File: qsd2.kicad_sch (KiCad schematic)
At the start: 72 parts, among them J1 5-1814832-1, J2 5-1814832-1, J3 Conn_02x08_Odd_Even, J4 SJ-3524-SMT, J5 B4B-XH-A_LF__SN_, U1 SN74LVC1G14DBV, U10 GALI-39, U11 SN74LVC1G14DBV, U12 LM4040DBZ-2.5, U13 LM4040DBZ-2.5, U2 SN74LVC1G14DBV, U3 SN74CBT3253, U4 SN74AC74PW, U5 AD8226ARZ-R7, U6 AD8226ARZ-R7, U9 UA78M05IDCYR

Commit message: V1.2 to fab.
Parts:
- removed R16: DNP, Resistor_SMD:R_1206_3216Metric, symbol Device:R_Small_US
- removed R19: 4.7k, Resistor_SMD:R_1206_3216Metric, symbol Device:R_Small_US
- removed U12, U13: LM4040DBZ-2.5, Package_TO_SOT_SMD:SOT-23, symbol Reference_Voltage:LM4040DBZ-2.5
- added C26: 1uF, Capacitor_SMD:C_1206_3216Metric, symbol Device:C_Small
- added U7: AP7343, Package_TO_SOT_SMD:SOT-23-5, symbol AP7343-25W5-7:AP7343
- R18: value 4.7k -> 2.2k
- R23, R24: value 2.61k -> 10k
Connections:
- net REF_Q is gone; now on net REF_V: C27.1, U6.6 (REF)
- net 5V_FILT: now also C23.1, U7.1 (VIN), U7.3 (EN); no longer R18.2
- net GND: now also R18.2, C26.2, U7.2 (GND)
- net at C20.2, R14.2: now also J4.2; no longer J4.3
- net at C21.2, R13.1: now also J4.3; no longer J4.2
- net REF_I renamed REF_V
- net REF_V: now also C26.1, U7.5 (VOUT); no longer C23.1
- no-connect marks 5 -> 6
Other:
- note removed: "Option for using a single reference source"
- moved on the sheet: C23, R18

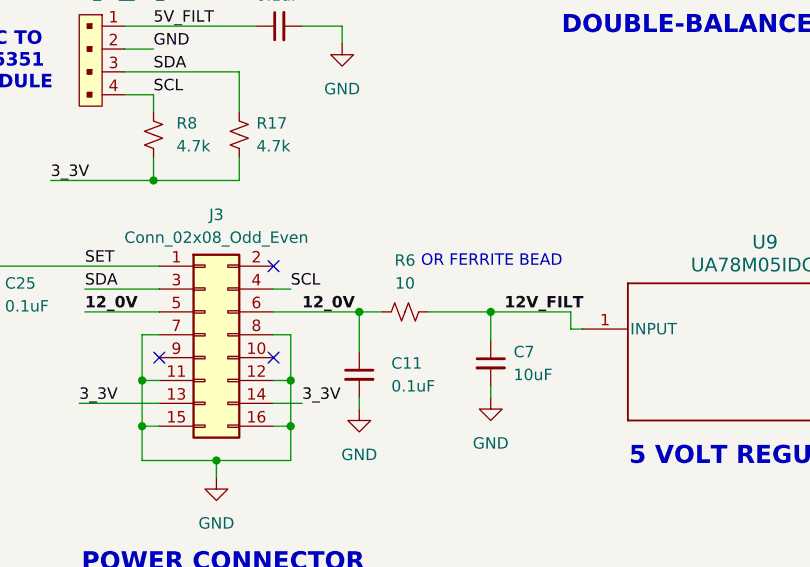
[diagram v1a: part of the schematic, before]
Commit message: Changed 10 ohm resistor to 20.  Fixed missing component value.
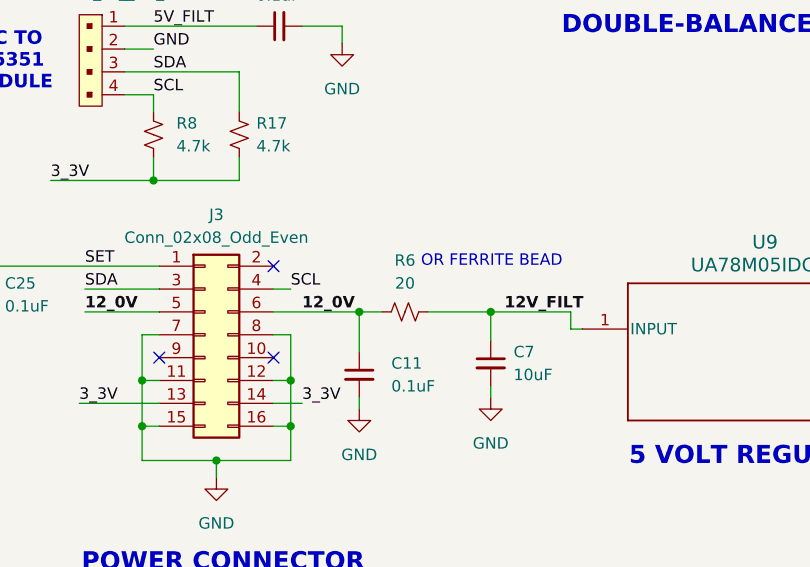
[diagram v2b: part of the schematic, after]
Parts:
- R6: value 10 -> 20
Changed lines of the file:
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@@
 	(title_block
 		(title "QSD2EZ with Divide-by-Two Quadrature Double-Balanced")
-		(date "2026-07-02")
+		(date "2026-07-21")
 		(rev "1.2")
 	)
@@
 			)
 		)
-		(property "Value" "10"
+		(property "Value" "20"
 			(at 67.945 163.83 90)
 			(show_name no)

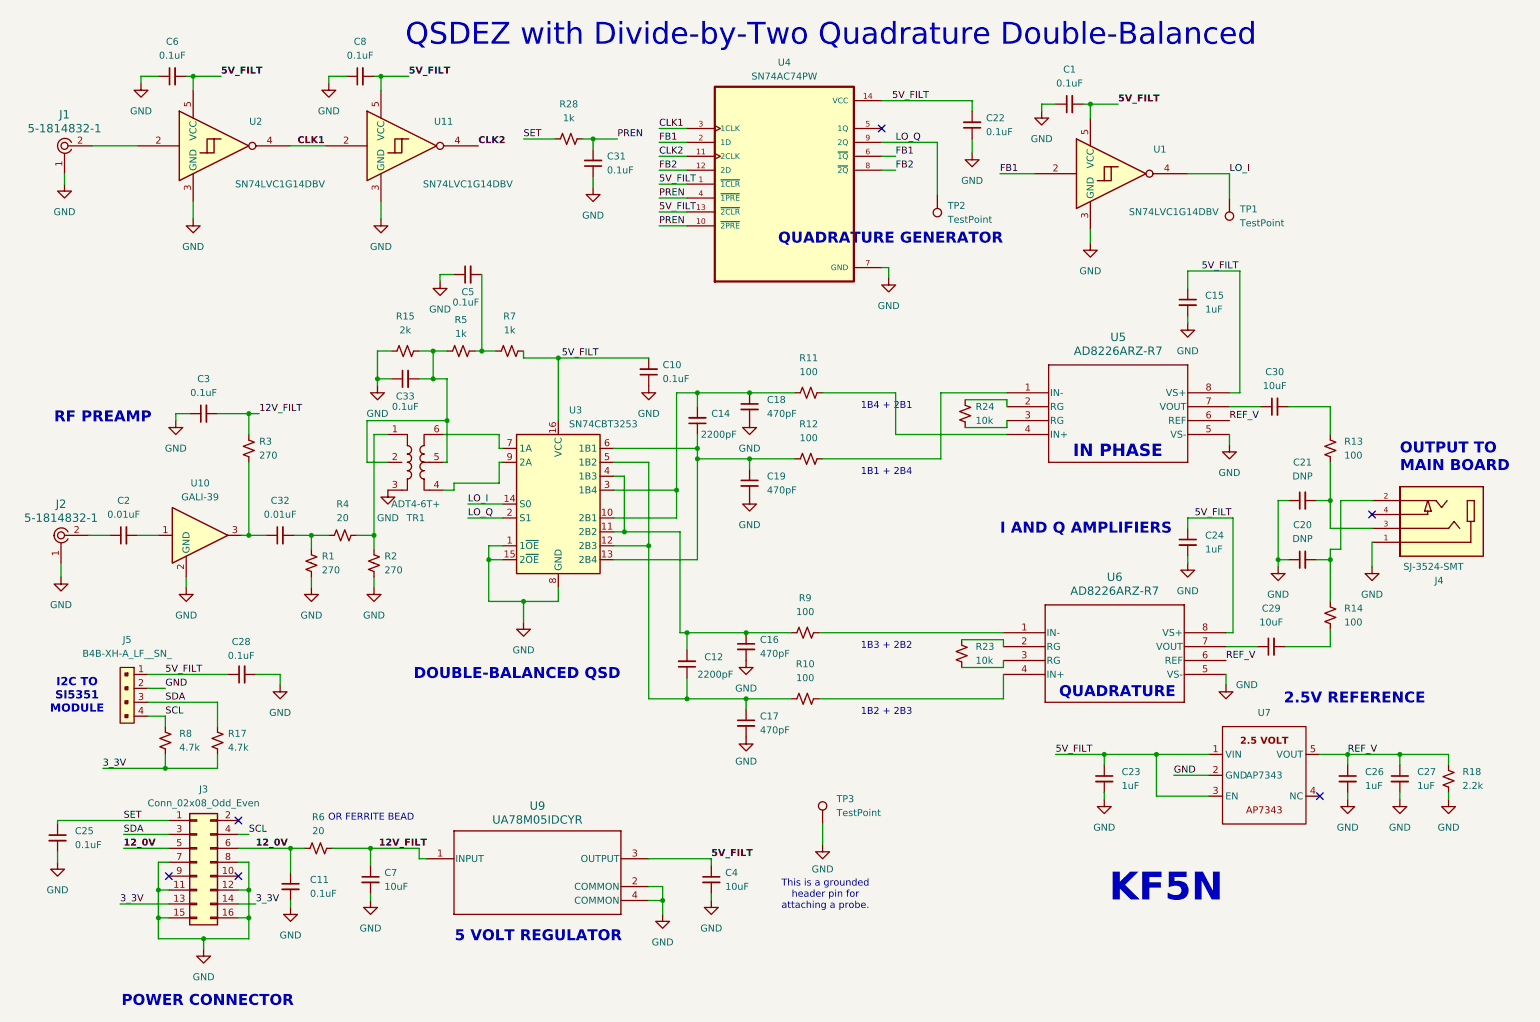
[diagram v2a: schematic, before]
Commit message: Cleaned up minor details in schematic.
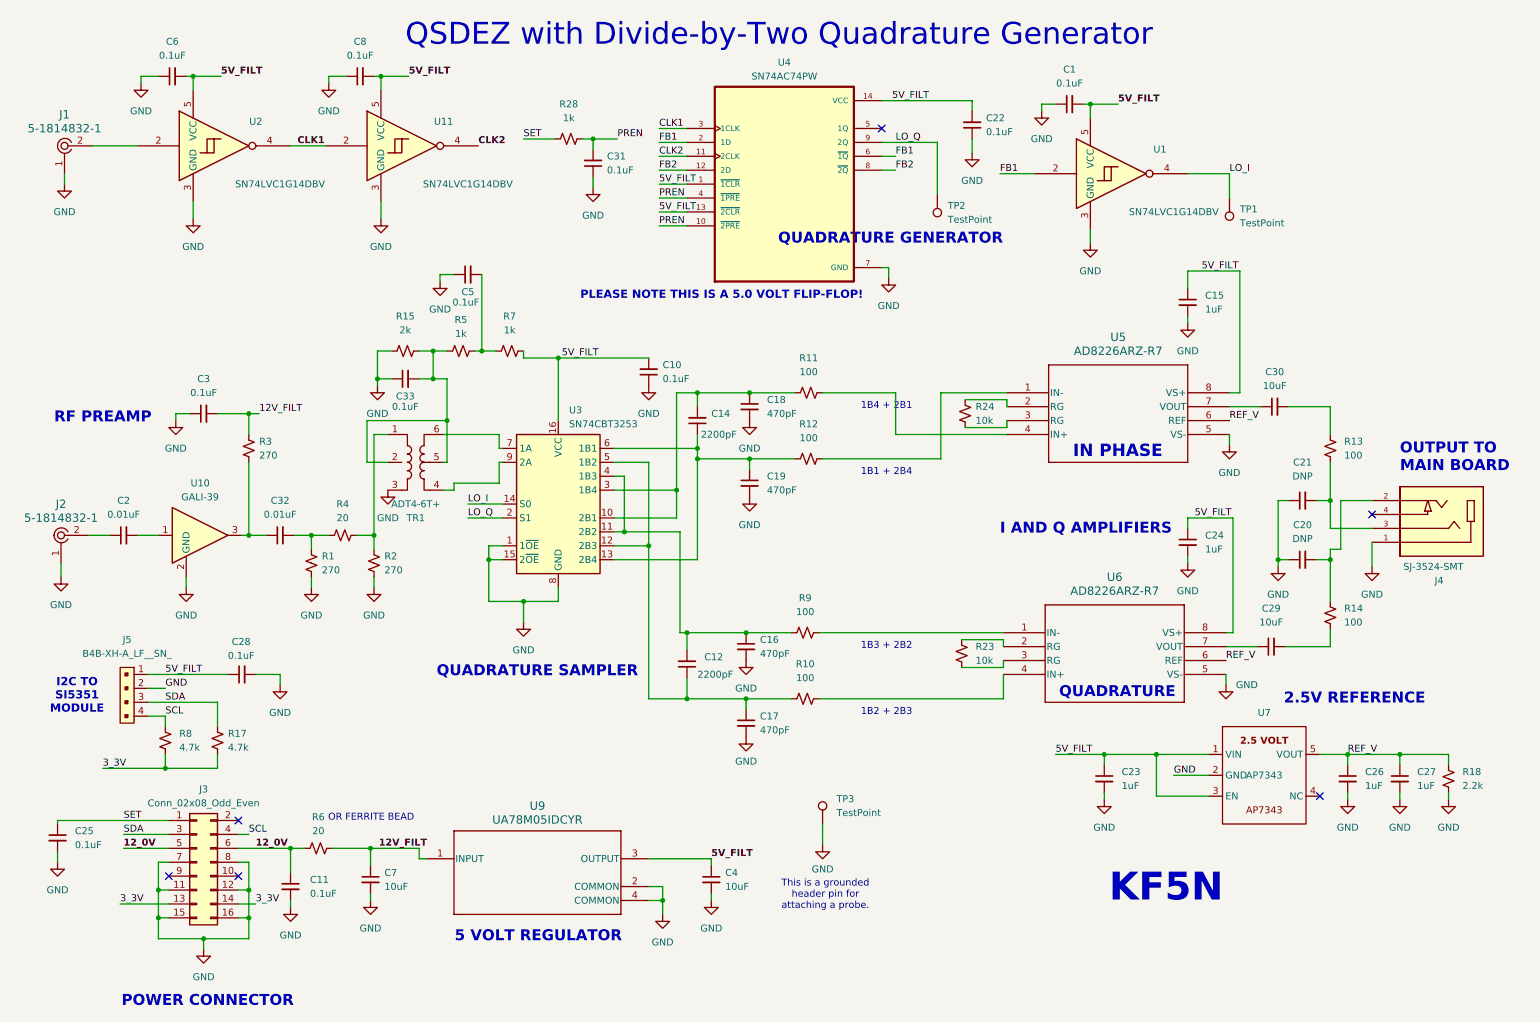
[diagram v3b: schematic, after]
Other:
- note added: "PLEASE NOTE THIS IS A 5.0 VOLT FLIP-FLOP!"
- note added: "QSDEZ with Divide-by-Two Quadrature Generator"
- note added: "QUADRATURE SAMPLER"
- note removed: "DOUBLE-BALANCED QSD"
- note removed: "QSDEZ with Divide-by-Two Quadrature Double-Balanced"
- title: QSD2EZ with Divide-by-Two Quadrature Double-Balanced -> QSD2EZ with Divide-by-Two Quadrature Generator
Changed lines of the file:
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@@
 	(paper "A4")
 	(title_block
-		(title "QSD2EZ with Divide-by-Two Quadrature Double-Balanced")
+		(title "QSD2EZ with Divide-by-Two Quadrature Generator")
 		(date "2026-07-21")
 		(rev "1.2")
@@
 		)
 	)
-	(text "DOUBLE-BALANCED QSD"
-		(exclude_from_sim no)
-		(at 85.344 136.398 0)
+	(text "QUADRATURE SAMPLER"
+		(exclude_from_sim no)
+		(at 89.535 135.89 0)
 		(effects
 			(font
@@
 			)
 			(justify left bottom)
+		)
+	)
+	(text "PLEASE NOTE THIS IS A 5.0 VOLT FLIP-FLOP!"
+		(exclude_from_sim no)
+		(at 141.605 66.04 0)
+		(effects
+			(font
+				(size 1.5 1.5)
+				(thickness 0.254)
+				(bold yes)
+			)
 		)
 	)
@@
 		)
 	)
-	(text "QSDEZ with Divide-by-Two Quadrature Double-Balanced"
+	(text "QSDEZ with Divide-by-Two Quadrature Generator"
 		(exclude_from_sim no)
 		(at 83.82 20.828 0)

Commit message: Updated PDF schematic.
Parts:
- U4: value SN74AC74PW -> MC74LCX74DR2G
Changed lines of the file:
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@@
 		(fields_autoplaced yes)
 		(property "Reference" "U4"
-			(at 153.035 23.495 0)
+			(at 153.035 22.86 0)
 			(show_name no)
 			(do_not_autoplace no)
@@
 			)
 		)
-		(property "Value" "SN74AC74PW"
-			(at 153.035 26.035 0)
+		(property "Value" "MC74LCX74DR2G"
+			(at 153.035 25.4 0)
 			(show_name no)
 			(do_not_autoplace no)
